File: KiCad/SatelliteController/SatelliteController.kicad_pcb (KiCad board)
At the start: 2 copper layers, 150 x 100 mm, 141 parts, among them J1 CONN_ICSP, J13 CONN_7SEG, J15 CONN_RS485, J2 CONN_USB, J3 USB_B_Micro, J4 DC_IN, J5 TO_CONVERTER, J6 FROM_CONVERTER, J7 CONN_STATUS_PANEL, J8 CONN_PANEL_BAORD_2, J9 CONN_PANEL_BAORD_1, Q1 TJ8S06M3L, Q2 TJ8S06M3L, Q3 2SC3325-Y, SW1 SW_Push, SW11 SW_Push, SW17 SW_Push, SW18 SW_Push, SW19 SW_Push, SW2 SW_Push, SW20 SW_Push, SW21 SW_Push, SW22 SW_Push, SW23 SW_Push, SW24 SW_Push, SW25 SW_Push, U1 FT232RL, U2 ATMEGA2560-16AUR, U3 NJM7805SDL1, U4 INA219BIDCNT, U5 INA219BIDCNT, U7 24LC256, U8 LTC485CN8#PBF, Y1 HUSG-16.000-20

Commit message: 残った手動制御を削除
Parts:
- removed U7: 24LC256, Package_DIP:DIP-8_W7.62mm
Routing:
- net (no net): track 50.1 -> 0.00 mm, vias 2 -> 0
- net CONN_LED_5V: track 648.0 -> 635.6 mm
- net I2C_SCL: track 83.2 -> 74.5 mm, vias 5 -> 4
- net I2C_SDA: track 82.7 -> 74.6 mm, vias 5 -> 4
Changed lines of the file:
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@@
     )
   )
-  (footprint "Package_DIP:DIP-8_W7.62mm" (layer "F.Cu")
-    (at 143.830707 97.146793 90)
-    (descr "8-lead though-hole mounted DIP package, row spacing 7.62 mm (300 mils)")
-    (tags "THT DIP DIL PDIP 2.54mm 7.62mm 300mil")
-    (property "LCSC" "")
-    (property "Sheetfile" "Peripheral.kicad_sch")
-    (property "Sheetname" "Peripheral")
-    (property "ki_description" "I2C Serial EEPROM, 256Kb, DIP-8/SOIC-8/TSSOP-8/DFN-8")
-    (property "ki_keywords" "I2C Serial EEPROM")
-    (attr through_hole)
-    (fp_text reference "U7" (at 3.81 -2.33 90) (layer "F.SilkS")
-        (effects (font (size 1 1) (thickness 0.15)))
-    )
-    (fp_text value "24LC256" (at 3.81 9.95 90) (layer "F.Fab")
-        (effects (font (size 1 1) (thickness 0.15)))
-    )
-    (fp_text user "${REFERENCE}" (at 3.81 3.81 90) (layer "F.Fab")
-        (effects (font (size 1 1) (thickness 0.15)))
-    )
-    (fp_line (start 1.16 -1.33) (end 1.16 8.95)
-      (stroke (width 0.12) (type solid)) (layer "F.SilkS"))
-    (fp_line (start 1.16 8.95) (end 6.46 8.95)
-      (stroke (width 0.12) (type solid)) (layer "F.SilkS"))
-    (fp_line (start 2.81 -1.33) (end 1.16 -1.33)
-      (stroke (width 0.12) (type solid)) (layer "F.SilkS"))
-    (fp_line (start 6.46 -1.33) (end 4.81 -1.33)
-      (stroke (width 0.12) (type solid)) (layer "F.SilkS"))
-    (fp_line (start 6.46 8.95) (end 6.46 -1.33)
-      (stroke (width 0.12) (type solid)) (layer "F.SilkS"))
-    (fp_arc (start 4.81 -1.33) (mid 3.81 -0.33) (end 2.81 -1.33)
-      (stroke (width 0.12) (type solid)) (layer "F.SilkS"))
-    (fp_line (start -1.1 -1.55) (end -1.1 9.15)
-      (stroke (width 0.05) (type solid)) (layer "F.CrtYd"))
-    (fp_line (start -1.1 9.15) (end 8.7 9.15)
-      (stroke (width 0.05) (type solid)) (layer "F.CrtYd"))
-    (fp_line (start 8.7 -1.55) (end -1.1 -1.55)
-      (stroke (width 0.05) (type solid)) (layer "F.CrtYd"))
-    (fp_line (start 8.7 9.15) (end 8.7 -1.55)
-      (stroke (width 0.05) (type solid)) (layer "F.CrtYd"))
-    (fp_line (start 0.635 -0.27) (end 1.635 -1.27)
-      (stroke (width 0.1) (type solid)) (layer "F.Fab"))
-    (fp_line (start 0.635 8.89) (end 0.635 -0.27)
-      (stroke (width 0.1) (type solid)) (layer "F.Fab"))
-    (fp_line (start 1.635 -1.27) (end 6.985 -1.27)
-      (stroke (width 0.1) (type solid)) (layer "F.Fab"))
-    (fp_line (start 6.985 -1.27) (end 6.985 8.89)
-      (stroke (width 0.1) (type solid)) (layer "F.Fab"))
-    (fp_line (start 6.985 8.89) (end 0.635 8.89)
-      (stroke (width 0.1) (type solid)) (layer "F.Fab"))
-    (pad "1" thru_hole rect (at 0 0 90) (size 1.6 1.6) (drill 0.8) (layers "*.Cu" "*.Mask")
-      (net 1 "GND") (pinfunction "A0") (pintype "input"))
-    (pad "2" thru_hole oval (at 0 2.54 90) (size 1.6 1.6) (drill 0.8) (layers "*.Cu" "*.Mask")
-      (net 1 "GND") (pinfunction "A1") (pintype "input"))
-    (pad "3" thru_hole oval (at 0 5.08 90) (size 1.6 1.6) (drill 0.8) (layers "*.Cu" "*.Mask")
-      (net 1 "GND") (pinfunction "A2") (pintype "input"))
-    (pad "4" thru_hole oval (at 0 7.62 90) (size 1.6 1.6) (drill 0.8) (layers "*.Cu" "*.Mask")
-      (net 1 "GND") (pinfunction "GND") (pintype "power_in"))
-    (pad "5" thru_hole oval (at 7.62 7.62 90) (size 1.6 1.6) (drill 0.8) (layers "*.Cu" "*.Mask")
-      (net 49 "I2C_SDA") (pinfunction "SDA") (pintype "bidirectional"))
-    (pad "6" thru_hole oval (at 7.62 5.08 90) (size 1.6 1.6) (drill 0.8) (layers "*.Cu" "*.Mask")
-      (net 48 "I2C_SCL") (pinfunction "SCL") (pintype "input"))
-    (pad "7" thru_hole oval (at 7.62 2.54 90) (size 1.6 1.6) (drill 0.8) (layers "*.Cu" "*.Mask")
-      (net 1 "GND") (pinfunction "WP") (pintype "input"))
-    (pad "8" thru_hole oval (at 7.62 0 90) (size 1.6 1.6) (drill 0.8) (layers "*.Cu" "*.Mask")
-      (net 35 "CONN_LED_5V") (pinfunction "VCC") (pintype "power_in"))
-    (model "${KICAD6_3DMODEL_DIR}/Package_DIP.3dshapes/DIP-8_W7.62mm.wrl"
-      (offset (xyz 0 0 0))
-      (scale (xyz 1 1 1))
-      (rotate (xyz 0 0 0))
-    )
-  )
   (footprint "Capacitor_SMD:C_1206_3216Metric_Pad1.33x1.80mm_HandSolder" (layer "F.Cu")
     (at 174.6 58.4 -90)
@@
     (style (thickness 0.15) (arrow_length 1.27) (text_position_mode 0) (extension_height 0.58642) (extension_offset 0.5) keep_text_aligned)
   )
-  (segment (start 112.2 49) (end 110.680707 47.480707) (width 0.2) (layer "F.Cu") (net 0))
-  (segment (start 130.444301 71.148199) (end 130.444301 72.326092) (width 0.2) (layer "F.Cu") (net 0))
-  (segment (start 130.209457 59.590543) (end 119.618914 49) (width 0.2) (layer "F.Cu") (net 0))
-  (segment (start 119.618914 49) (end 112.2 49) (width 0.2) (layer "F.Cu") (net 0))
-  (segment (start 110.680707 42.061793) (end 109.730707 41.111793) (width 0.2) (layer "F.Cu") (net 0))
-  (segment (start 130.444301 72.326092) (end 127.695359 75.075034) (width 0.2) (layer "F.Cu") (net 0))
-  (segment (start 110.680707 47.480707) (end 110.680707 42.061793) (width 0.2) (layer "F.Cu") (net 0))
-  (segment (start 131.230707 70.361793) (end 130.444301 71.148199) (width 0.2) (layer "F.Cu") (net 0))
-  (via (at 130.209457 59.590543) (size 0.5) (drill 0.3) (layers "F.Cu" "B.Cu") (net 0))
-  (via (at 131.230707 70.361793) (size 0.5) (drill 0.3) (layers "F.Cu" "B.Cu") (net 0))
-  (segment (start 132.980707 68.611793) (end 131.230707 70.361793) (width 0.2) (layer "B.Cu") (net 0))
-  (segment (start 130.209457 59.590543) (end 132.980707 62.361793) (width 0.2) (layer "B.Cu") (net 0))
-  (segment (start 132.980707 62.361793) (end 132.980707 68.611793) (width 0.2) (layer "B.Cu") (net 0))
   (segment (start 125.155707 107.911249) (end 125.155707 109.646793) (width 0.25) (layer "F.Cu") (net 1))
   (segment (start 131.938 82.375911) (end 130.950805 81.388716) (width 0.25) (layer "F.Cu") (net 1))
@@
   (segment (start 129.980707 75.111793) (end 130.480707 75.111793) (width 0.25) (layer "B.Cu") (net 35))
   (segment (start 90.46 75.75) (end 88.91 77.3) (width 1) (layer "B.Cu") (net 35))
-  (segment (start 138.730707 99.746793) (end 138.730707 94.626793) (width 0.5) (layer "B.Cu") (net 35))
   (segment (start 140.030707 101.046793) (end 138.730707 99.746793) (width 0.5) (layer "B.Cu") (net 35))
   (segment (start 79.46 65.75) (end 79.46 75.74) (width 1) (layer "B.Cu") (net 35))
@@
   (segment (start 118.191201 71.714472) (end 112.730707 77.174966) (width 0.25) (layer "B.Cu") (net 35))
   (segment (start 95.85 38.611793) (end 108 38.611793) (width 1) (layer "B.Cu") (net 35))
-  (segment (start 138.730707 94.626793) (end 143.830707 89.526793) (width 0.5) (layer "B.Cu") (net 35))
   (segment (start 56.96 65.75) (end 56.96 75.75) (width 1) (layer "B.Cu") (net 35))
   (segment (start 113.213207 97.344293) (end 115.330707 99.461793) (width 2) (layer "B.Cu") (net 35))
@@
   (via (at 112.35 72.8) (size 0.5) (drill 0.3) (layers "F.Cu" "B.Cu") (net 48))
   (via (at 162.130707 80.846793) (size 0.5) (drill 0.3) (layers "F.Cu" "B.Cu") (net 48))
-  (via (at 148.130707 81.121793) (size 0.5) (drill 0.3) (layers "F.Cu" "B.Cu") (net 48))
   (via (at 140.505457 82.837043) (size 0.5) (drill 0.3) (layers "F.Cu" "B.Cu") (net 48))
   (via (at 167.130707 80.846793) (size 0.5) (drill 0.3) (layers "F.Cu" "B.Cu") (net 48))
   (segment (start 135.980707 76.861793) (end 139.980707 80.861793) (width 0.2) (layer "B.Cu") (net 48))
-  (segment (start 148.130707 81.121793) (end 148.910707 81.901793) (width 0.2) (layer "B.Cu") (net 48))
   (segment (start 139.980707 82.312293) (end 140.505457 82.837043) (width 0.2) (layer "B.Cu") (net 48))
   (segment (start 162.130707 80.846793) (end 167.130707 80.846793) (width 0.2) (layer "B.Cu") (net 48))
@@
   (segment (start 123.480707 66.611793) (end 133.730707 76.861793) (width 0.2) (layer "B.Cu") (net 48))
   (segment (start 118.380707 66.611793) (end 123.480707 66.611793) (width 0.2) (layer "B.Cu") (net 48))
-  (segment (start 148.910707 81.901793) (end 148.910707 89.526793) (width 0.2) (layer "B.Cu") (net 48))
   (segment (start 148.540707 83.861793) (end 150.630707 81.771793) (width 0.2) (layer "F.Cu") (net 49))
   (segment (start 167.130707 82.096793) (end 167.455707 81.771793) (width 0.2) (layer "F.Cu") (net 49))
@@
   (via (at 112.35 73.8) (size 0.5) (drill 0.3) (layers "F.Cu" "B.Cu") (net 49))
   (via (at 167.130707 82.096793) (size 0.5) (drill 0.3) (layers "F.Cu" "B.Cu") (net 49))
-  (via (at 150.630707 81.771793) (size 0.5) (drill 0.3) (layers "F.Cu" "B.Cu") (net 49))
   (via (at 162.153399 82.087937) (size 0.5) (drill 0.3) (layers "F.Cu" "B.Cu") (net 49))
   (via (at 138.480707 82.861793) (size 0.5) (drill 0.3) (layers "F.Cu" "B.Cu") (net 49))
@@
   (segment (start 112.35 73.8) (end 112.35 73.7425) (width 0.2) (layer "B.Cu") (net 49))
   (segment (start 137.980707 79.611793) (end 137.980707 82.361793) (width 0.2) (layer "B.Cu") (net 49))
-  (segment (start 151.450707 82.591793) (end 151.450707 89.526793) (width 0.2) (layer "B.Cu") (net 49))
-  (segment (start 150.630707 81.771793) (end 151.450707 82.591793) (width 0.2) (layer "B.Cu") (net 49))
   (segment (start 135.030707 92.161793) (end 135.030707 97.734293) (width 0.2) (layer "F.Cu") (net 52))
   (segment (start 134.730707 78.796293) (end 134.581207 78.646793) (width 0.2) (layer "F.Cu") (net 52))

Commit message: 7セグ用のコネクタを移動
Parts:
- moved J13 74.9 mm to (150.8, 91.8), turned to 0 degrees
- moved R20 40.7 mm to (143.1, 91.5)
- moved R19 36.0 mm to (141.1, 91.5)
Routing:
- net 7SEG_DIO: track 72.8 -> 23.2 mm, vias 3 -> 2
- net 7SEG_CLK: track 73.2 -> 25.2 mm, vias 3 -> 0
- net CONN_LED_5V: track 635.6 -> 606.6 mm
- net GND: vias 284 -> 283

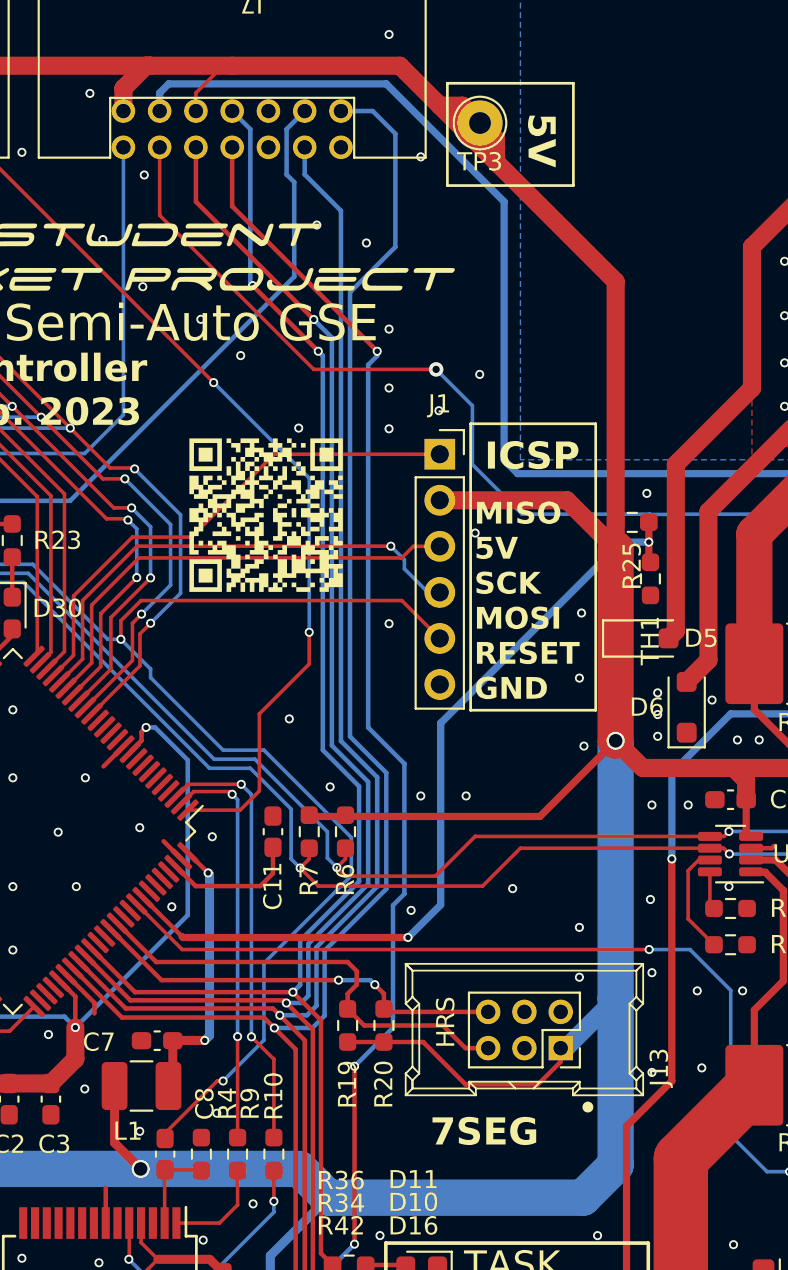
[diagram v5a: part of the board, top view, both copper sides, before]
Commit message: 7セグ用コネクタを6Pから14Pの空いているピンに押し込んだ
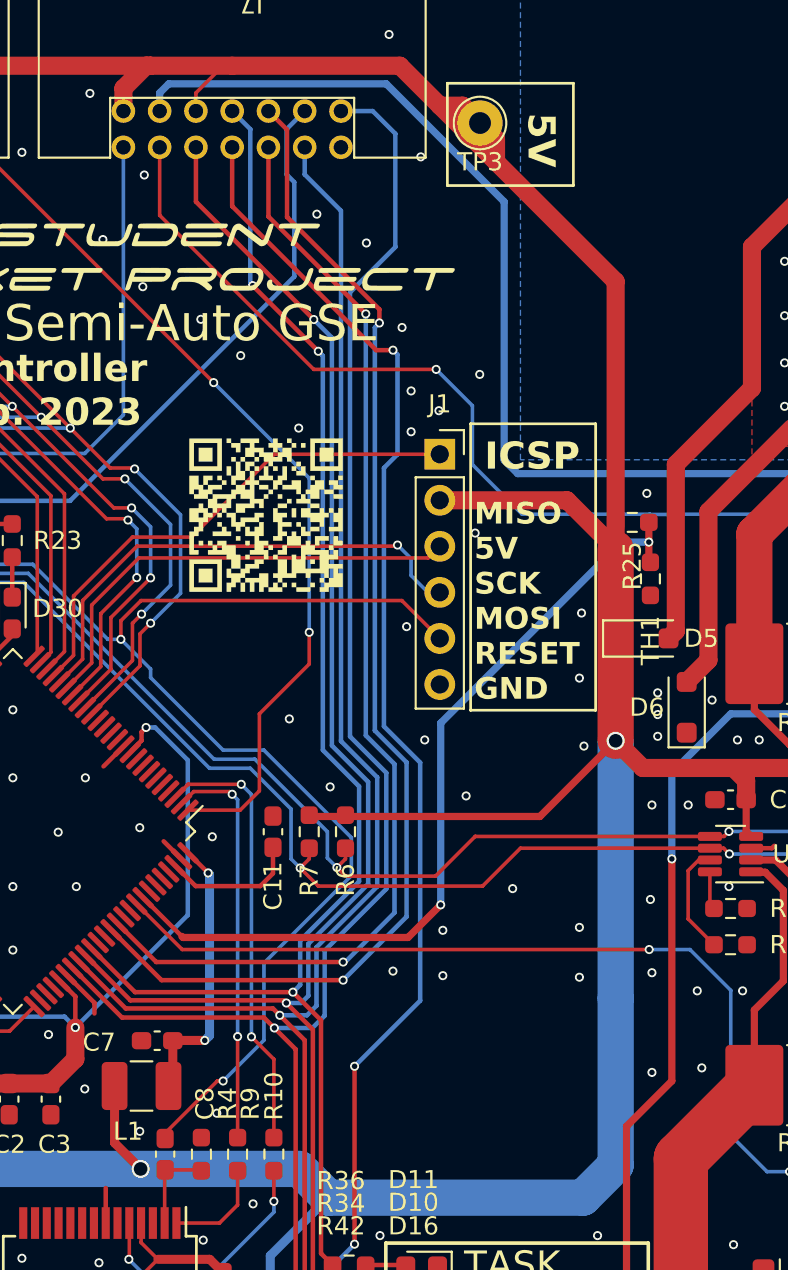
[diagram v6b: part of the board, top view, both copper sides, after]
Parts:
- removed J13: CONN_7SEG, TSRP_Connector_Hirose:DF51A-6DP-2DSA
- removed R19, R20: 10kR, Resistor_SMD:R_0603_1608Metric_Pad0.98x0.95mm_HandSolder
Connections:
- J7 pad 5: unconnected-(J7-Pin_5-Pad5) -> 7SEG_CLK
- J7 pad 6: unconnected-(J7-Pin_6-Pad6) -> 7SEG_DIO
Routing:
- net 7SEG_DIO: track 23.2 -> 66.7 mm
- net 7SEG_CLK: track 25.2 -> 62.4 mm, vias 0 -> 2
- net CONN_LED_5V: track 606.6 -> 588.5 mm
- net CONN_LED_USB_ACCESS: track 86.8 -> 88.3 mm
- net GND: vias 283 -> 284
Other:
- board text removed: "7SEG"

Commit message: コネクタをまとめた
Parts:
- removed J9: CONN_PANEL_BAORD_1, TSRP_Connector_Hirose:DF51A-18DP-2DS
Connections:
- J8 pad 10: unconnected-(J8-Pin_10-Pad10) -> CTL_RUN
- J8 pad 19: unconnected-(J8-Pin_19-Pad19) -> CTL_SAFETY
- J8 pad 21: unconnected-(J8-Pin_21-Pad21) -> CTL_PURGE
- J8 pad 8: unconnected-(J8-Pin_8-Pad8) -> CTL_KILL
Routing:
- net CONN_LED_5V: track 588.5 -> 528.8 mm
- net CTL_PURGE: track 98.8 -> 128.2 mm
- net CTL_KILL: track 248.6 -> 277.0 mm
- net CTL_RUN: track 233.7 -> 261.6 mm
- net CTL_SAFETY: track 160.3 -> 150.2 mm
- net GND: vias 284 -> 289
